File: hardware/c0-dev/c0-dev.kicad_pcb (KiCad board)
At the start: 2 copper layers, 160 x 68 mm, 454 parts, among them J101 2913730000, J102 2913730000, J103 2913730000, J104 2913730000, J105 2913730000, J106 2913730000, J107 2913730000, J108 2913730000, J109 2913730000, J110 2913730000, J111 2913730000, J112 2913730000, J201 RJ45_LED_Shielded, J401 TAG_CONNECT, J402 PinHeader_2.54mm, Q1001 BSS138P, Q1002 BSS138P, Q1003 BSS138P, Q1004 BSS138P, Q1005 BSS138P, Q1006 BSS138P, Q1007 BSS138P, Q1008 BSS138P, Q1009 BSS138P, Q701 BSS138P, Q702 BSS138P, U1001 TCA9555PWR, U1002 TPS4H000A-Q1, U1003 TPS4H000A-Q1, U1101 LM5160A, U1102 LM317L, U1301 TPS4H000A-Q1, U201 LAN8720A, U301 AP63203WU, U302 TPS2378, U303 TPS54360DDA, U304 TLP175A, U401 TCA9555PWR, U402 W25Q128JVP, U403 RP2350A, U404 TPS3820-33DBV, U501 B0505S-1WR3, U502 ISO1540, U503 ISO1540, U504 TMP117xxDRV, U505 AMS1117-3.3, U506 TMP117xxDRV, U507 ADS1015IDGS, U508 ADS1015IDGS, U601 ADS1015IDGS, U602 ADS1015IDGS, U603 ADS1015IDGS, U604 ADS1015IDGS, U701 B0505S-1WR3, U702 ISO6741, U703 ISO6741, U704 ADS1220xPW, U705 ADS1220xPW, U801 B0505S-1WR3, U802 ISO1044BD, U803 TLP175A, U901 ISO1212, U902 ISO1212, U903 ISO1212, U904 ISO1212, Y401 ABM8-272-T3 (12Mhz)

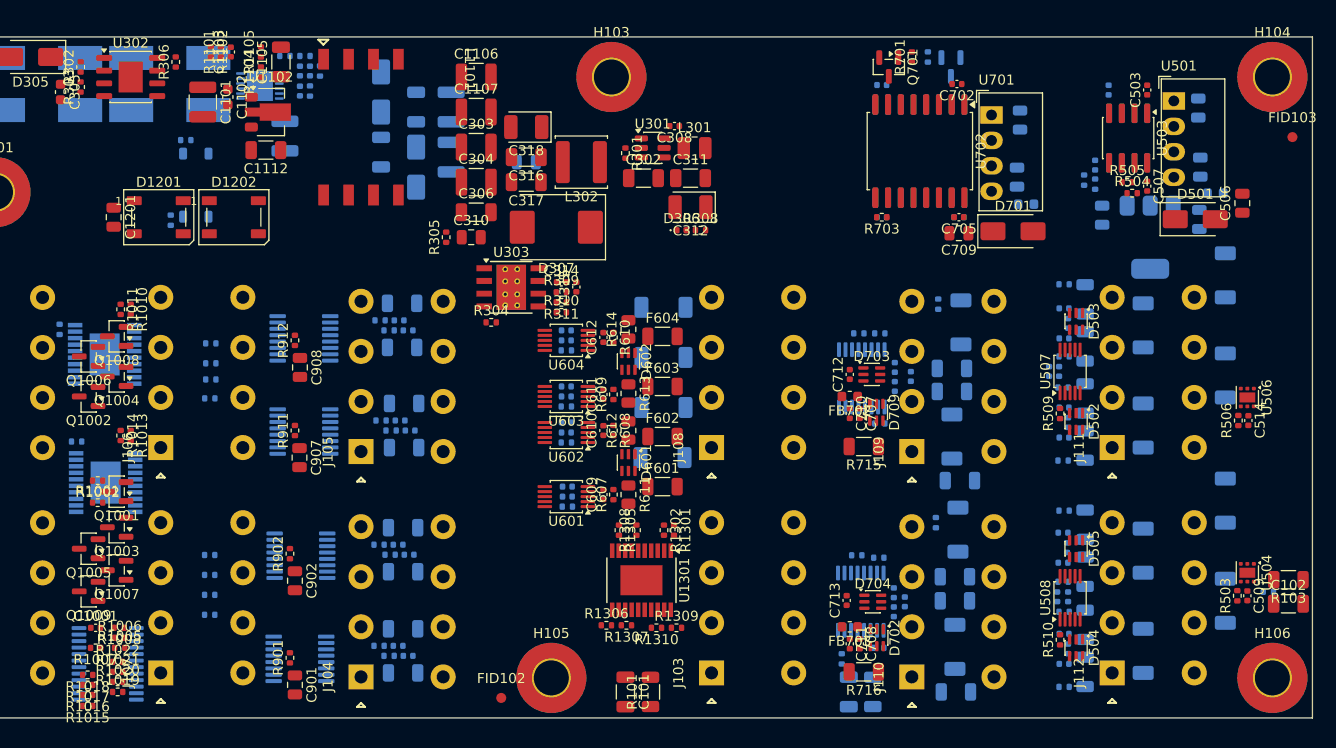
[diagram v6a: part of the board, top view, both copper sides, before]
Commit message: added leds, removed screen
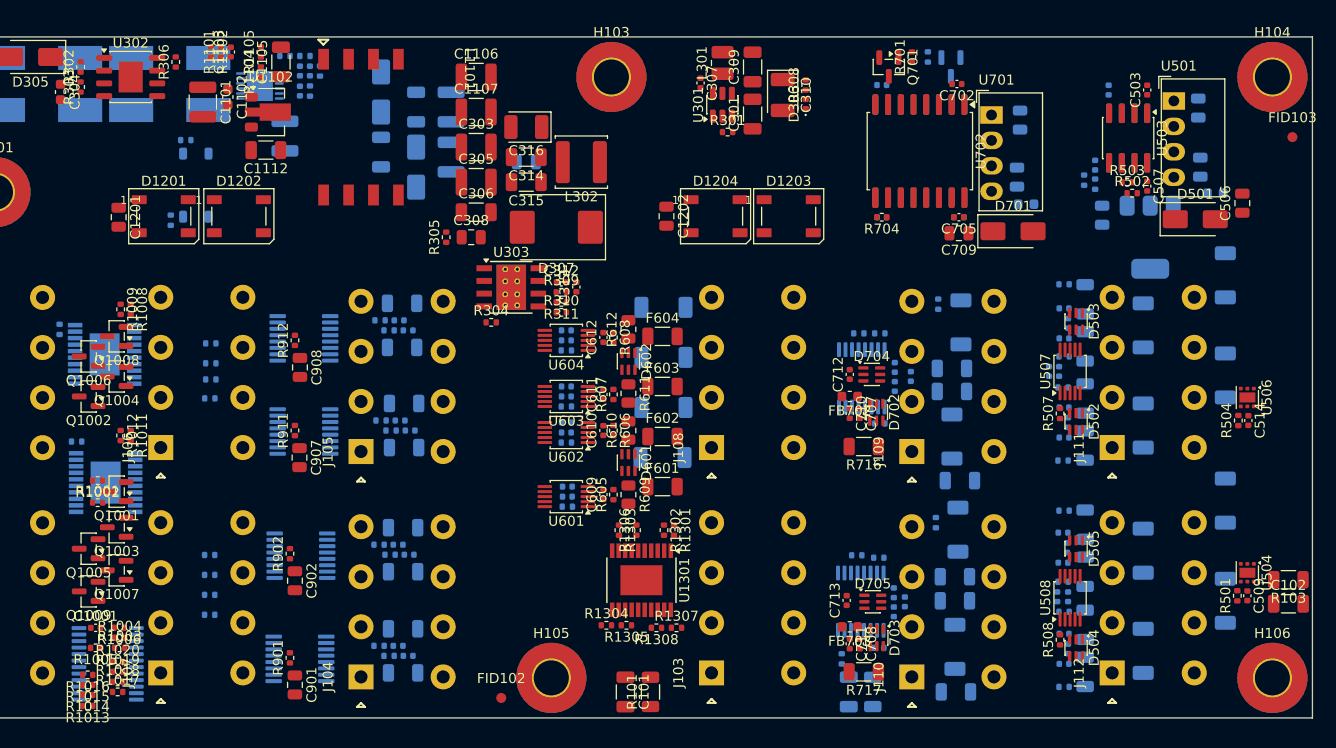
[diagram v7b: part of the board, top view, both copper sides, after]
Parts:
- removed C527: 10uF, Capacitor_SMD:C_0805_2012Metric
- removed R527: 0, Resistor_SMD:R_0402_1005Metric
- added C1202: 10uF, Capacitor_SMD:C_0805_2012Metric, F.Cu at (155.5, 79.9)
- added D1203: WS2812B, LED_SMD:LED_WS2812B_PLCC4_5.0x5.0mm_P3.2mm, F.Cu at (167.7, 79.9)
- added D1204: WS2812B, LED_SMD:LED_WS2812B_PLCC4_5.0x5.0mm_P3.2mm, F.Cu at (160.4, 79.9)
- moved R308 17.9 mm to (169.4, 66.8), turned to 90 degrees
- moved D306 17.7 mm to (169.4, 68.7), turned to 90 degrees
- moved C310 14.5 mm to (167.1, 67.8), turned to -90 degrees
- moved C309 12.7 mm to (164.1, 65.0), turned to 90 degrees
- moved C301 12.6 mm to (164.1, 69.7), turned to 90 degrees
- moved R301 10.4 mm to (161.6, 71.5), turned to 0 degrees
- moved L301 8.95 mm to (161.1, 64.6), turned to 90 degrees
- moved U301 8.18 mm to (161.1, 68.8), turned to 90 degrees
- moved C307 5.02 mm to (158.9, 66.6), turned to -90 degrees
- moved D1201 0.51 mm to (105.3, 79.9)
- moved D1202 0.51 mm to (112.8, 79.9)
- moved C1201 0.50 mm to (100.8, 80.0)
- renumbered C302 to C301, C301 to C302, C305 to C304, C304 to C305, C308 to C307, C310 to C308, C311 to C309, C312 to C310, C313 to C311, C314 to C312, C315 to C313, C316 to C314, C317 to C315, C318 to C316, D709 to D702, D702 to D703, D703 to D704, D704 to D705, D705 to D706, D706 to D707, D707 to D708, D708 to D709, R1005 to R1003, R1006 to R1004, R1007 to R1005, R1008 to R1006, R1009 to R1007, R1010 to R1008, R1011 to R1009, R1012 to R1010, R1013 to R1011, R1014 to R1012, R1015 to R1013, R1016 to R1014, R1017 to R1015, R1018 to R1016, R1019 to R1017, R1020 to R1018, R1021 to R1019, R1022 to R1020, R1023 to R1021, R1024 to R1022, R1025 to R1023, R1026 to R1024, R1027 to R1025, R1028 to R1026, R1029 to R1027, R1030 to R1028, R1305 to R1303, R1306 to R1304, R1307 to R1305, R1308 to R1306, R1309 to R1307, R1310 to R1308, R503 to R501, R504 to R502, R505 to R503, R506 to R504, R507 to R505, R508 to R506, R509 to R507, R510 to R508, R511 to R509, R512 to R510, R513 to R511, R514 to R512, R515 to R513, R516 to R514, R517 to R515, R518 to R516, R519 to R517, R520 to R518, R521 to R519, R522 to R520, R523 to R521, R524 to R522, R525 to R523, R526 to R524, R603 to R601, R604 to R602, R605 to R603, R606 to R604, R607 to R605, R608 to R606, R609 to R607, R610 to R608, R611 to R609, R612 to R610, R613 to R611, R614 to R612, R719 to R703, R703 to R704, R704 to R705, R705 to R706, R706 to R707, R707 to R708, R708 to R709, R709 to R710, R710 to R711, R711 to R712, R712 to R713, R713 to R714, R714 to R715, R715 to R716, R716 to R717, R717 to R718, R718 to R719
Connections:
- net /frontend_temp/GND_TC renamed /GND_TC
- C504 pad 1: Net-(U501-+Vout) -> unconnected-(C504-Pad1)
- C504 pad 2: /frontend_temp/GND -> GND
- C505 pad 1: /frontend_temp/+3.3V -> +3.3V
- C505 pad 2: /frontend_temp/GND -> GND
- C506 pad 2: /frontend_temp/GND -> GND
- C507 pad 1: /frontend_temp/+3.3V -> +3.3V
- C507 pad 2: /frontend_temp/GND -> GND
- C508 pad 1: /frontend_temp/+3.3V -> +3.3V
- C508 pad 2: /frontend_temp/GND -> GND
- C509 pad 1: /frontend_temp/+3.3V -> +3.3V
- C509 pad 2: /frontend_temp/GND -> GND
- C510 pad 1: /frontend_temp/+3.3V -> +3.3V
- C510 pad 2: /frontend_temp/GND -> GND
- C511 pad 1: /frontend_temp/+3.3V -> +3.3V
- C511 pad 2: /frontend_temp/GND -> GND
- C512 pad 1: /frontend_temp/+3.3V -> +3.3V
- C512 pad 2: /frontend_temp/GND -> GND
- C513 pad 1: /frontend_temp/+3.3V -> +3.3V
- C513 pad 2: /frontend_temp/GND -> GND
- C514 pad 1: /frontend_temp/+3.3V -> +3.3V
- C514 pad 2: /frontend_temp/GND -> GND
- C515 pad 2: /frontend_temp/GND -> GND
- C517 pad 2: /frontend_temp/GND -> GND
- C518 pad 2: /frontend_temp/GND -> GND
- C520 pad 2: /frontend_temp/GND -> GND
- C521 pad 2: /frontend_temp/GND -> GND
- C523 pad 2: /frontend_temp/GND -> GND
- C524 pad 2: /frontend_temp/GND -> GND
- C526 pad 2: /frontend_temp/GND -> GND
- D1202 pad 2: unconnected-(D1202-DOUT-Pad2) -> Net-(D1202-DOUT)
- D502 pad 1: /frontend_temp/GND -> GND
- D502 pad 2: /frontend_temp/+3.3V -> +3.3V
- D502 pad 4: /frontend_temp/GND -> GND
- D502 pad 5: /frontend_temp/+3.3V -> +3.3V
- D503 pad 1: /frontend_temp/GND -> GND
- D503 pad 2: /frontend_temp/+3.3V -> +3.3V
- D503 pad 4: /frontend_temp/GND -> GND
- D503 pad 5: /frontend_temp/+3.3V -> +3.3V
- D504 pad 1: /frontend_temp/GND -> GND
- D504 pad 2: /frontend_temp/+3.3V -> +3.3V
- D504 pad 4: /frontend_temp/GND -> GND
- D504 pad 5: /frontend_temp/+3.3V -> +3.3V
- D505 pad 1: /frontend_temp/GND -> GND
- D505 pad 2: /frontend_temp/+3.3V -> +3.3V
- D505 pad 4: /frontend_temp/GND -> GND
- D505 pad 5: /frontend_temp/+3.3V -> +3.3V
- D506 pad 2: /frontend_temp/GND -> GND
- D507 pad 1: /frontend_temp/GND -> GND
- D508 pad 2: /frontend_temp/GND -> GND
- D509 pad 1: /frontend_temp/GND -> GND
- D510 pad 2: /frontend_temp/GND -> GND
- D511 pad 1: /frontend_temp/GND -> GND
- D512 pad 2: /frontend_temp/GND -> GND
- D513 pad 1: /frontend_temp/GND -> GND
- R501 pad 1: /frontend_temp/+3.3V -> +3.3V
- R502 pad 2: /frontend_temp/+3.3V -> +3.3V
- R503 pad 2: /frontend_temp/+3.3V -> +3.3V
- R504 pad 1: /frontend_temp/GND -> GND
- R505 pad 2: /frontend_temp/+3.3V -> +3.3V
- R506 pad 2: /frontend_temp/+3.3V -> +3.3V
- R507 pad 1: /frontend_temp/GND -> GND
- R508 pad 1: /frontend_temp/+3.3V -> +3.3V
- R517 pad 2: /frontend_temp/+3.3V -> +3.3V
- R518 pad 1: /frontend_temp/GND -> GND
- R519 pad 2: /frontend_temp/+3.3V -> +3.3V
- R520 pad 1: /frontend_temp/GND -> GND
- R521 pad 2: /frontend_temp/+3.3V -> +3.3V
- R522 pad 1: /frontend_temp/GND -> GND
- R523 pad 2: /frontend_temp/+3.3V -> +3.3V
- R524 pad 1: /frontend_temp/GND -> GND
- U501 pad 3: /frontend_temp/GND -> GND
- U502 pad 2: /MCU/I2C0.SDA -> /frontend_temp/SDA
- U502 pad 3: /MCU/I2C0.SCL -> /frontend_temp/SCL
- U502 pad 5: /frontend_temp/GND -> GND
- U502 pad 8: /frontend_temp/+3.3V -> +3.3V
- U503 pad 2: /MCU/I2C1.SDA -> /frontend_temp/SDA_400K
- U503 pad 3: /MCU/I2C1.SCL -> /frontend_temp/SCL_400K
- U503 pad 5: /frontend_temp/GND -> GND
- U503 pad 8: /frontend_temp/+3.3V -> +3.3V
- U504 pad 2: /frontend_temp/GND -> GND
- U504 pad 5: /frontend_temp/+3.3V -> +3.3V
- U504 pad 7: /frontend_temp/TC3- -> /frontend_temp/TC2-
- U505 pad 1: /frontend_temp/GND -> GND
- U505 pad 2: /frontend_temp/+3.3V -> +3.3V
- U506 pad 2: /frontend_temp/GND -> GND
- U506 pad 5: /frontend_temp/+3.3V -> +3.3V
- U507 pad 3: /frontend_temp/GND -> GND
- U507 pad 8: /frontend_temp/+3.3V -> +3.3V
- U508 pad 3: /frontend_temp/GND -> GND
- U508 pad 8: /frontend_temp/+3.3V -> +3.3V
